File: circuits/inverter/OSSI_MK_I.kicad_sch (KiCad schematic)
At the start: 0 parts

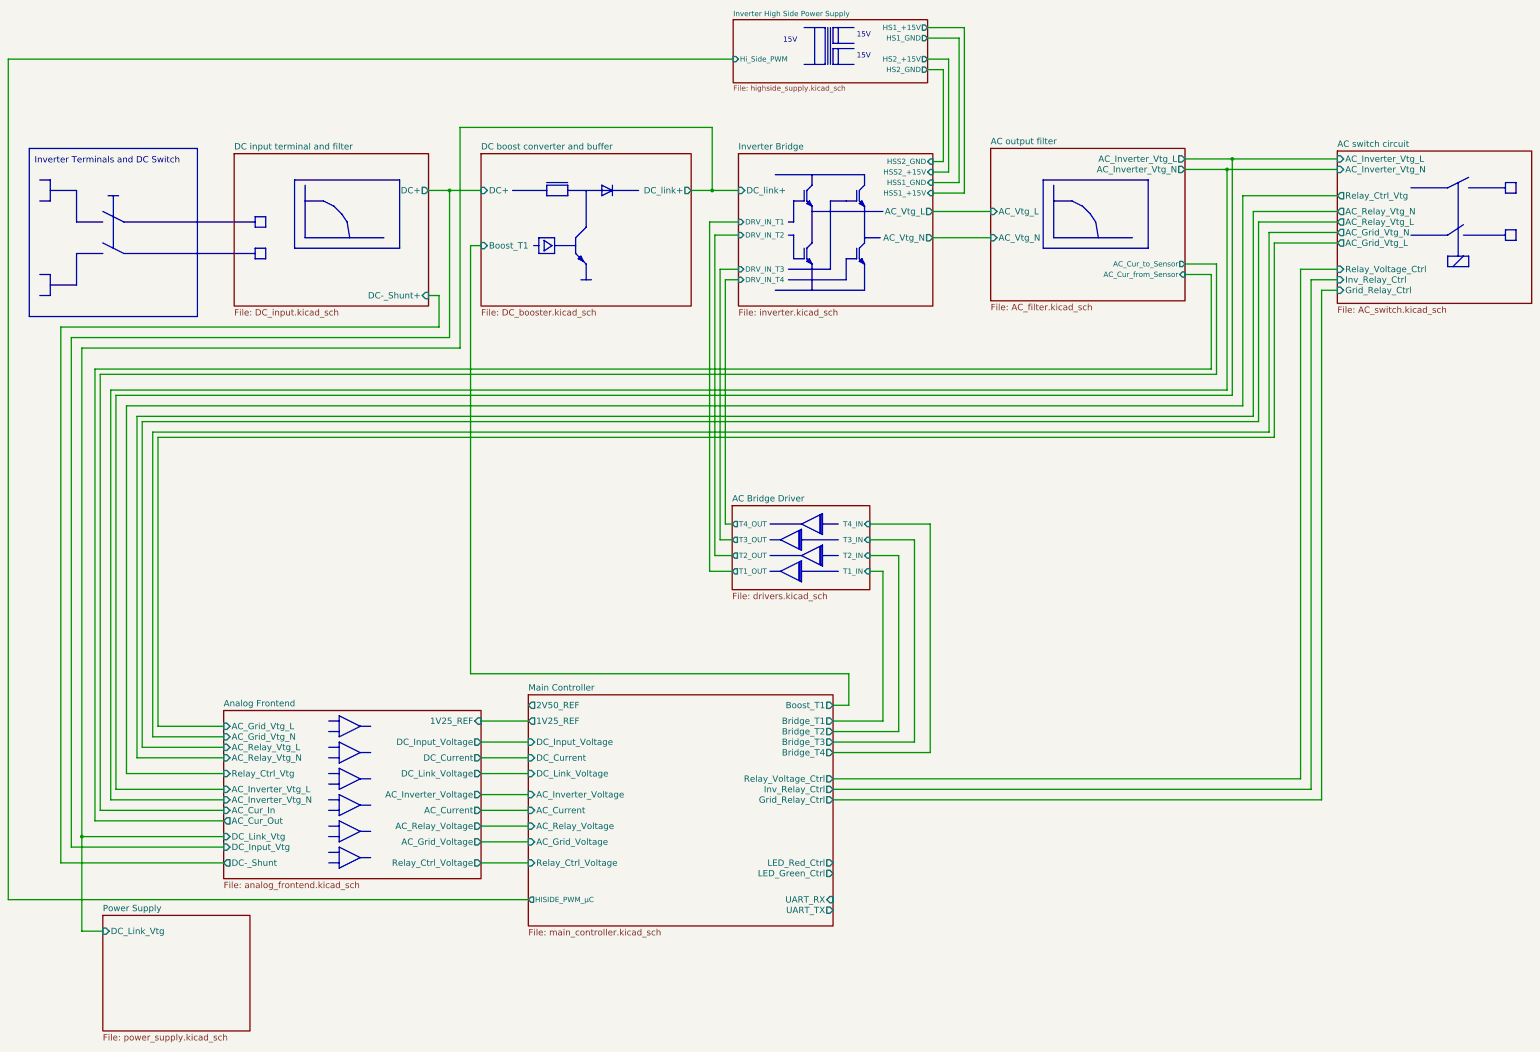
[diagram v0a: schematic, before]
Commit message: converts libraries to Kicad 6 format, updates bridge driver
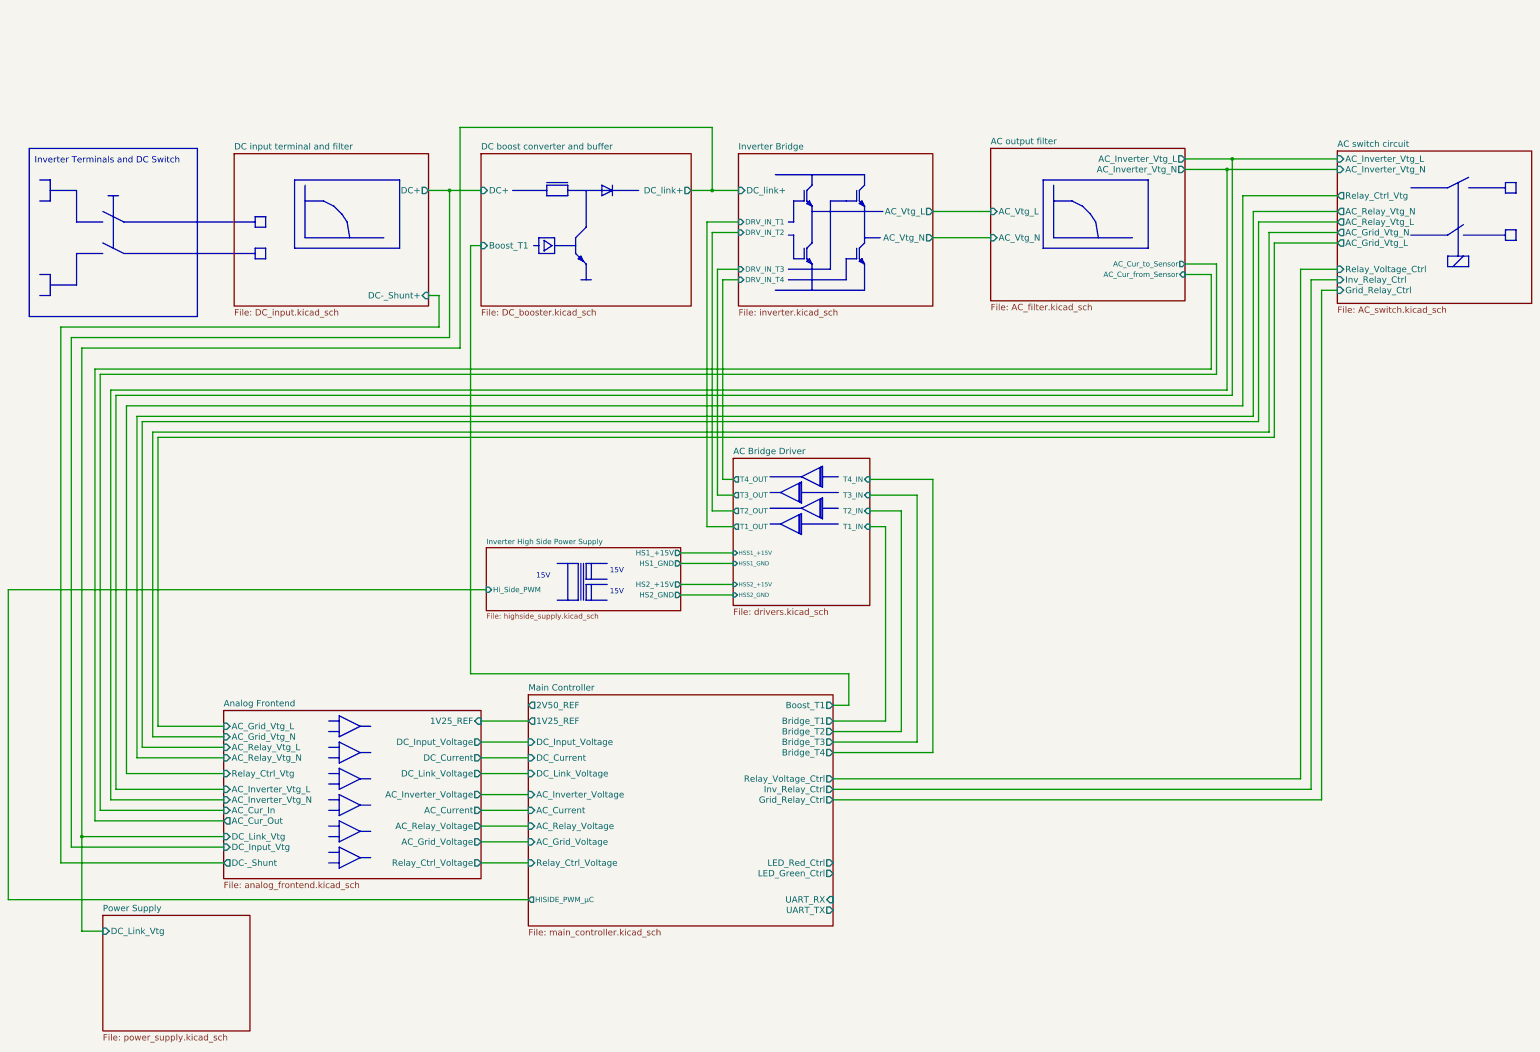
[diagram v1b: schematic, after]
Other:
- sheet AC Bridge Driver  ports: added HSS1_+15V, HSS1_GND, HSS2_+15V, HSS2_GND; removed none
- sheet Inverter Bridge ports: added none; removed HSS1_+15V, HSS1_GND, HSS2_+15V, HSS2_GND

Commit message: updates circuits, adds linear regulator NCP1117
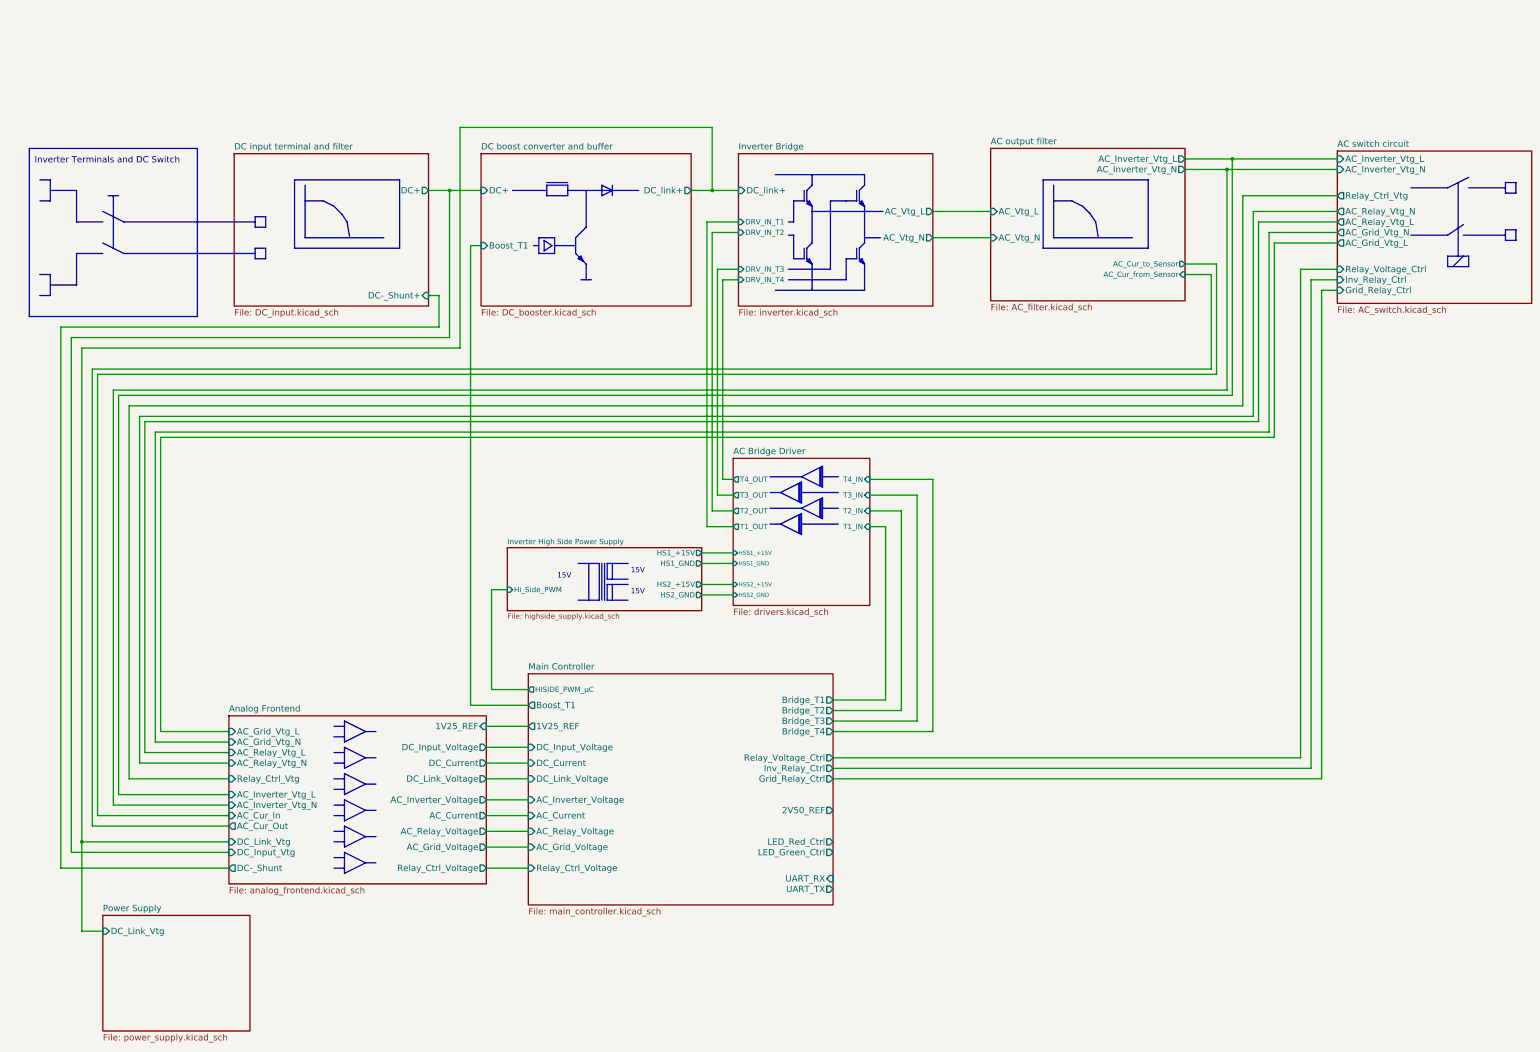
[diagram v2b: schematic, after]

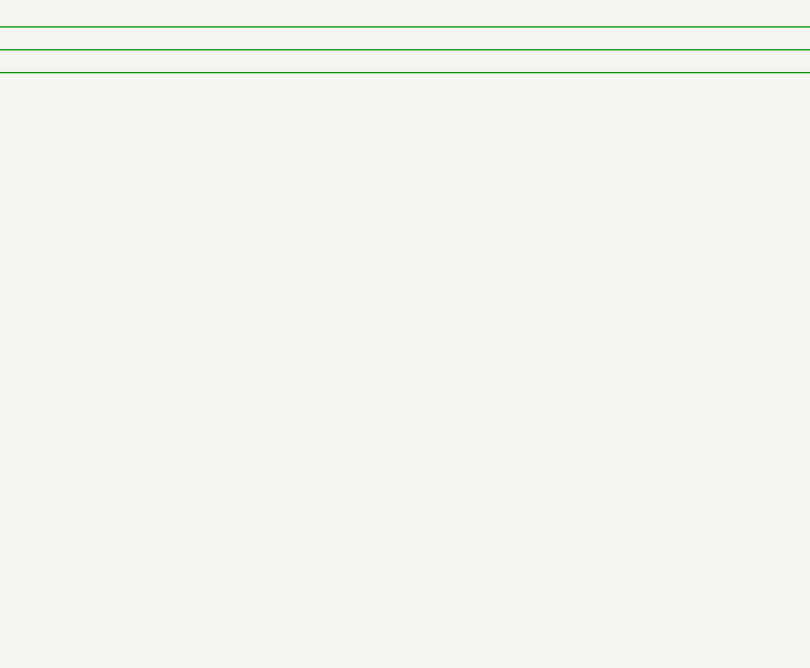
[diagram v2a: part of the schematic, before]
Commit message: adds interface schematic and NodeMCU symbol for it
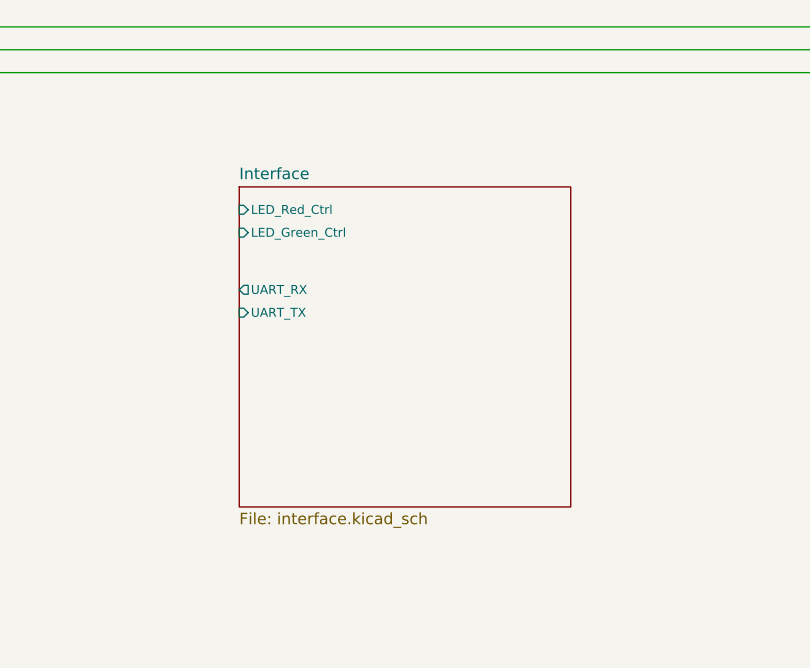
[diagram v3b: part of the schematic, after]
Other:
- added sheet Interface (interface.kicad_sch)
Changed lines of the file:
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@@
+    )
+  )
+  (sheet (at 247.65 228.6) (size 36.83 35.56) (fields_autoplaced)
+    (stroke (width 0.1524) (type solid) (color 0 0 0 0))
+    (fill (color 0 0 0 0.0000))
+    (property "Sheet name" "Interface" (id 0) (at 247.65 227.8884 0)
+      (effects (font (size 1.27 1.27)) (justify left bottom))
+    )
+    (property "Sheet file" "interface.kicad_sch" (id 1) (at 247.65 264.7446 0)
+      (effects (font (size 1.27 1.27)) (justify left top))
+    )
+    (pin "LED_Red_Ctrl" input (at 247.65 231.14 180)
+      (effects (font (size 0.9906 0.9906)) (justify left))
+    )
+    (pin "UART_RX" output (at 247.65 240.03 180)
+      (effects (font (size 0.9906 0.9906)) (justify left))
+    )
+    (pin "LED_Green_Ctrl" input (at 247.65 233.68 180)
+      (effects (font (size 0.9906 0.9906)) (justify left))
+    )
+    (pin "UART_TX" input (at 247.65 242.57 180)
+      (effects (font (size 0.9906 0.9906)) (justify left))
     )
   )
@@
     (path "/00000000-0000-0000-0000-000056d9c18a" (page "11"))
     (path "/00000000-0000-0000-0000-000056d9c195" (page "12"))
+    (path "/cab3d5bb-ff0d-4636-b5aa-2e3bdeaa7d38" (page "13"))
   )
   (symbol_instances
@@
       (reference "#PWR?") (unit 1) (value "GND") (footprint "")
     )
+    (path "/cab3d5bb-ff0d-4636-b5aa-2e3bdeaa7d38/24fd0624-2007-4122-82ab-d6982361155f"
+      (reference "#PWR?") (unit 1) (value "+3V3") (footprint "")
+    )
     (path "/00000000-0000-0000-0000-000056d9d1ec/39f18c5d-a191-414a-8e3d-baa12b17ccd3"
       (reference "#PWR?") (unit 1) (value "GND") (footprint "")
     )
+    (path "/cab3d5bb-ff0d-4636-b5aa-2e3bdeaa7d38/4536eb1c-3ee1-40e4-bf2a-a50e43a75300"
+      (reference "#PWR?") (unit 1) (value "+3V3") (footprint "")
+    )
     (path "/00000000-0000-0000-0000-000056d9d1ec/4a6a5826-af06-429d-8371-d254b7144429"
       (reference "#PWR?") (unit 1) (value "+3V3") (footprint "")
@@
       (reference "#PWR?") (unit 1) (value "GND") (footprint "")
     )
+    (path "/cab3d5bb-ff0d-4636-b5aa-2e3bdeaa7d38/5cc2558d-561c-4033-bb6a-58ed22ed60fe"
+      (reference "#PWR?") (unit 1) (value "GND") (footprint "")
+    )
     (path "/00000000-0000-0000-0000-000056d9c185/60306fc6-2f05-4323-ac12-24dac2e47345"
       (reference "#PWR?") (unit 1) (value "Earth_Protective") (footprint "")
@@
       (reference "#PWR?") (unit 1) (value "+3V3") (footprint "")
     )
+    (path "/cab3d5bb-ff0d-4636-b5aa-2e3bdeaa7d38/a8f53d73-e8e5-4f6b-b6ba-c54f6c8f0ffa"
+      (reference "#PWR?") (unit 1) (value "GND") (footprint "")
+    )
     (path "/00000000-0000-0000-0000-000056d9c185/acfce14d-664f-4864-9245-c60ab2efdb5e"
       (reference "#PWR?") (unit 1) (value "GND") (footprint "")
@@
       (reference "#PWR?") (unit 1) (value "+3V3") (footprint "")
     )
+    (path "/cab3d5bb-ff0d-4636-b5aa-2e3bdeaa7d38/db090e56-d20c-4650-8ee4-96538a65021b"
+      (reference "#PWR?") (unit 1) (value "GND") (footprint "")
+    )
     (path "/00000000-0000-0000-0000-000056d9d1ec/f7051609-0a75-451f-a24f-5dcb366680b0"
       (reference "#PWR?") (unit 1) (value "GND") (footprint "")
@@
       (reference "D?") (unit 1) (value "Diode") (footprint "")
     )
+    (path "/cab3d5bb-ff0d-4636-b5aa-2e3bdeaa7d38/20e91ff9-7fe9-431f-adfc-c8eb609ce138"
+      (reference "H?") (unit 1) (value "LED") (footprint "")
+    )
+    (path "/cab3d5bb-ff0d-4636-b5aa-2e3bdeaa7d38/2f9ebda7-e579-43a6-b79d-08e2052404b8"
+      (reference "H?") (unit 1) (value "LED") (footprint "")
+    )
     (path "/00000000-0000-0000-0000-000056d9c195/00000000-0000-0000-0000-000058d8c008"
       (reference "K?") (unit 1) (value "OJE-SH-112HM") (footprint "")
@@
       (reference "Q?") (unit 1) (value "IGBT") (footprint "")
     )
+    (path "/cab3d5bb-ff0d-4636-b5aa-2e3bdeaa7d38/da062af7-c447-4676-abf1-3dd5aee197f5"
+      (reference "Q?") (unit 1) (value "NMOS") (footprint "")
+    )
+    (path "/cab3d5bb-ff0d-4636-b5aa-2e3bdeaa7d38/e4fbf319-9b1d-4cd1-a193-ee5f26329782"
+      (reference "Q?") (unit 1) (value "NMOS") (footprint "")
+    )
     (path "/00000000-0000-0000-0000-000056d9be97/00000000-0000-0000-0000-000058d7f88f"
       (reference "R?") (unit 1) (value "10") (footprint "")
@@
       (reference "R?") (unit 1) (value "220") (footprint "")
     )
+    (path "/cab3d5bb-ff0d-4636-b5aa-2e3bdeaa7d38/05c98823-39c3-4e60-b2d4-bea04efc21da"
+      (reference "R?") (unit 1) (value "220") (footprint "")
+    )
     (path "/00000000-0000-0000-0000-000056d9d1ec/05f9f019-22ce-45e7-b901-b07b44309d40"
       (reference "R?") (unit 1) (value "Resistor") (footprint "")
@@
       (reference "R?") (unit 1) (value "Resistor") (footprint "")
     )
+    (path "/cab3d5bb-ff0d-4636-b5aa-2e3bdeaa7d38/2bddfd85-ac0c-4edc-b4d5-bea8cac8034c"
+      (reference "R?") (unit 1) (value "10k") (footprint "")
+    )
+    (path "/cab3d5bb-ff0d-4636-b5aa-2e3bdeaa7d38/3194626b-3fa9-4b75-9083-ffc943f9837f"
+      (reference "R?") (unit 1) (value "0") (footprint "")
+    )
     (path "/00000000-0000-0000-0000-000056d9d1ec/36517a78-427d-4081-90ae-088eec68fda2"
       (reference "R?") (unit 1) (value "45.3") (footprint "")
@@
       (reference "R?") (unit 1) (value "Resistor") (footprint "")
     )
+    (path "/00000000-0000-0000-0000-000056d9d692/5013f733-a331-49d0-82c4-189004e2283c"
+      (reference "R?") (unit 1) (value "10k") (footprint "")
+    )
     (path "/00000000-0000-0000-0000-000056d9d1ec/531ed155-8409-4b46-9d49-491653344012"
       (reference "R?") (unit 1) (value "Resistor") (footprint "")
@@
       (reference "R?") (unit 1) (value "45.3") (footprint "")
     )
+    (path "/cab3d5bb-ff0d-4636-b5aa-2e3bdeaa7d38/834cfa90-a32e-4ad2-9d19-256d41e10425"
+      (reference "R?") (unit 1) (value "220") (footprint "")
+    )
     (path "/00000000-0000-0000-0000-000056d9d1ec/8520746c-287c-4c7c-a6bd-13211ca98b9e"
       (reference "R?") (unit 1) (value "Resistor") (footprint "")
@@
       (reference "R?") (unit 1) (value "Resistor") (footprint "")
     )
+    (path "/cab3d5bb-ff0d-4636-b5aa-2e3bdeaa7d38/9928c283-c43d-4cf0-8279-acc1fefb1e7d"
+      (reference "R?") (unit 1) (value "10k") (footprint "")
+    )
     (path "/00000000-0000-0000-0000-000056d9d1ec/9e33e13a-e821-4041-8888-0ccd3e027740"
       (reference "R?") (unit 1) (value "45.3") (footprint "")
@@
       (reference "U?") (unit 1) (value "SN74LVC14") (footprint "")
     )
+    (path "/cab3d5bb-ff0d-4636-b5aa-2e3bdeaa7d38/8765685c-0431-4101-87c6-5c376195bd02"
+      (reference "U?") (unit 1) (value "NodeMCU") (footprint "")
+    )
     (path "/00000000-0000-0000-0000-000056d9d1ec/dc217ae5-0ff4-4377-9165-cb14842534ee"
